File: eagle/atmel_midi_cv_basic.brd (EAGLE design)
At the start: 101 x 82 mm, 46 parts, among them IC1 TL074P, Q2 2N3904, U1 ATMEGA328P_PDIP

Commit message: led fixed
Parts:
- R11: value 1k -> 1k5
- R4: value 1k8 -> 3k3
- moved VEL_LED 1.80 mm to (28.4, 24.1)
- moved Q2 1.27 mm to (30.5, 17.8)
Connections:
- removed net N$47: R25.2, VEL_LED.K
- new net N$24: Q2.3, R25.2
- net N$20: now also Q2.1, VEL_LED.K; no longer Q2.3, VEL_LED.A
- net N$21: now also VEL_LED.A; no longer Q2.1
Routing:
- net N$47: track 6.83 -> 0.00 mm
- net N$24: track 0.00 -> 3.81 mm
- net N$21: track 43.2 -> 39.4 mm
- net N$20: track 5.47 -> 6.56 mm
- net N$23: track 6.83 -> 5.74 mm
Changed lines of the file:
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@@
 <?xml version="1.0" encoding="utf-8"?>
 <!DOCTYPE eagle SYSTEM "eagle.dtd">
-<eagle version="7.1.0">
+<eagle version="7.2.0">
 <drawing>
 <settings>
@@
 <attribute name="OC_FARNELL" value="1667008" x="55.88" y="69.85" size="1.778" layer="27" display="off"/>
 </element>
-<element name="Q2" library="transistor-npn" package="TO92" value="2N3904" x="29.21" y="17.78" rot="R180"/>
+<element name="Q2" library="transistor-npn" package="TO92" value="2N3904" x="30.48" y="17.78" rot="R180"/>
 <element name="R1" library="rcl" package="0207/10" value="10k" x="19.05" y="67.31"/>
 <element name="R10" library="rcl" package="0207/10" value="1k" x="72.39" y="20.32"/>
-<element name="R11" library="rcl" package="0207/10" value="1k" x="46.355" y="45.466" rot="R180"/>
+<element name="R11" library="rcl" package="0207/10" value="1k5" x="46.355" y="45.466" rot="R180"/>
 <element name="R17" library="rcl" package="0207/10" value="10k" x="40.64" y="21.59" rot="R180"/>
 <element name="R18" library="rcl" package="0207/10" value="47k" x="37.338" y="27.686"/>
@@
 <element name="R26" library="rcl" package="0207/10" value="1k" x="19.05" y="37.084"/>
 <element name="R3" library="rcl" package="0207/10" value="270" x="74.93" y="46.99" rot="R180"/>
-<element name="R4" library="rcl" package="0207/10" value="1k8" x="40.64" y="13.716"/>
+<element name="R4" library="rcl" package="0207/10" value="3k3" x="40.64" y="13.716"/>
 <element name="R5" library="rcl" package="0207/10" value="3.3k" x="32.258" y="42.672" rot="R270"/>
 <element name="R6" library="pot" package="B64W" value="10k" x="53.34" y="25.4" rot="R90"/>
@@
 <element name="U1" library="SparkFun-DigitalIC" package="DIL28-3" value="ATMEGA328P_PDIP" x="60.96" y="60.96" rot="R180"/>
 <element name="VEL" library="erthenvar" package="ERTHENVAR-JACK-90DEG" value="AUDIO-JACK" x="66.04" y="0" rot="R180"/>
-<element name="VEL_LED" library="SparkFun-LED" package="LED5MM" value="" x="29.718" y="22.86"/>
+<element name="VEL_LED" library="SparkFun-LED" package="LED5MM" value="" x="28.448" y="24.13"/>
 </elements>
 <signals>
@@
 <wire x1="35.052" y1="55.118" x2="41.402" y2="60.198" width="0.8128" layer="16"/>
 </signal>
-<signal name="N$47">
-<contactref element="R25" pad="2"/>
-<contactref element="VEL_LED" pad="K"/>
-<wire x1="30.988" y1="22.86" x2="35.56" y2="17.78" width="0.8128" layer="16"/>
-</signal>
 <signal name="N$14">
 <contactref element="U$4" pad="6"/>
@@
 <wire x1="64.77" y1="57.15" x2="66.04" y2="53.34" width="0.8128" layer="16"/>
 </signal>
-<signal name="N$20">
-<contactref element="VEL_LED" pad="A"/>
-<contactref element="Q2" pad="3"/>
-<wire x1="28.448" y1="22.86" x2="30.48" y2="17.78" width="0.8128" layer="16"/>
-</signal>
 <signal name="N$21">
 <contactref element="IC1" pad="14"/>
-<contactref element="Q2" pad="1"/>
 <contactref element="IC1" pad="13"/>
-<wire x1="21.59" y1="25.4" x2="27.94" y2="17.78" width="0.8128" layer="16"/>
 <wire x1="21.209" y1="26.035" x2="21.59" y2="25.4" width="0.8128" layer="16"/>
 <wire x1="21.209" y1="40.005" x2="21.209" y2="26.035" width="0.8128" layer="16"/>
@@
 <wire x1="36.576" y1="41.91" x2="35.179" y2="41.148" width="0.8128" layer="16"/>
 <wire x1="36.576" y1="41.91" x2="39.116" y2="41.91" width="0.8128" layer="16"/>
+<contactref element="VEL_LED" pad="A"/>
+<wire x1="27.178" y1="24.13" x2="22.86" y2="24.13" width="0.8128" layer="16"/>
+<wire x1="22.86" y1="24.13" x2="21.59" y2="25.4" width="0.8128" layer="16"/>
 </signal>
 <signal name="N$22">
@@
 <contactref element="Q2" pad="2"/>
 <contactref element="R4" pad="1"/>
-<wire x1="33.274" y1="13.843" x2="29.21" y2="15.875" width="0.8128" layer="16"/>
+<wire x1="33.274" y1="13.843" x2="30.48" y2="15.875" width="0.8128" layer="16"/>
 <wire x1="35.56" y1="13.716" x2="33.274" y2="13.843" width="0.8128" layer="16"/>
 </signal>
@@
 <wire x1="65.024" y1="20.574" x2="67.31" y2="20.32" width="0.8128" layer="16"/>
 </signal>
+<signal name="N$20">
+<contactref element="Q2" pad="1"/>
+<contactref element="VEL_LED" pad="K"/>
+<wire x1="29.21" y1="17.78" x2="29.21" y2="23.622" width="0.8128" layer="16"/>
+<wire x1="29.21" y1="23.622" x2="29.718" y2="24.13" width="0.8128" layer="16"/>
+</signal>
+<signal name="N$24">
+<contactref element="Q2" pad="3"/>
+<contactref element="R25" pad="2"/>
+<wire x1="35.56" y1="17.78" x2="31.75" y2="17.78" width="0.8128" layer="16"/>
+</signal>
 </signals>

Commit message: playing scale to indicate midi channel by number of notes
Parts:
- R5: value 3.3k -> 3k3
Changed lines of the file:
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@@
 <?xml version="1.0" encoding="utf-8"?>
 <!DOCTYPE eagle SYSTEM "eagle.dtd">
-<eagle version="7.2.0">
+<eagle version="7.1.0">
 <drawing>
 <settings>
@@
 <element name="R3" library="rcl" package="0207/10" value="270" x="74.93" y="46.99" rot="R180"/>
 <element name="R4" library="rcl" package="0207/10" value="3k3" x="40.64" y="13.716"/>
-<element name="R5" library="rcl" package="0207/10" value="3.3k" x="32.258" y="42.672" rot="R270"/>
+<element name="R5" library="rcl" package="0207/10" value="3k3" x="32.258" y="42.672" rot="R270"/>
 <element name="R6" library="pot" package="B64W" value="10k" x="53.34" y="25.4" rot="R90"/>
 <element name="R7" library="rcl" package="0207/10" value="5k" x="59.69" y="33.02" rot="R90"/>

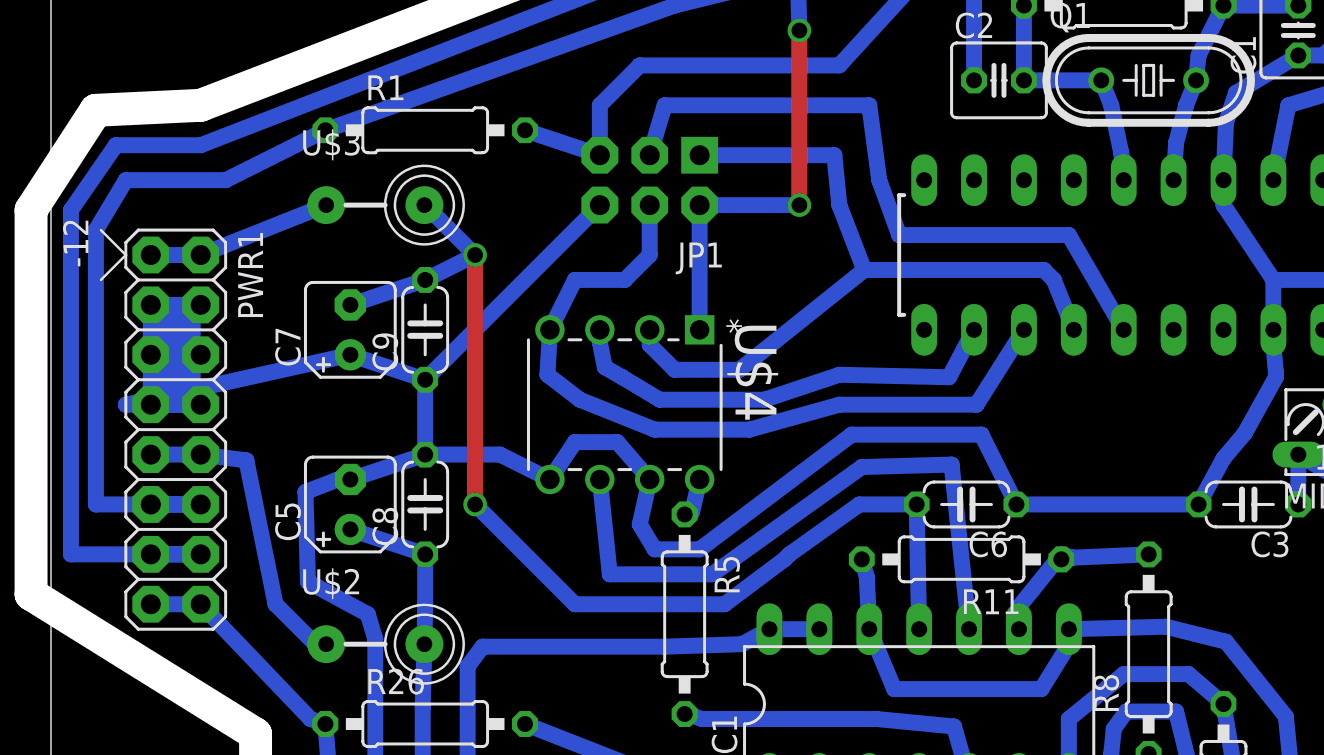
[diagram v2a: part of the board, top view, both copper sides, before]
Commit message: no neg supply
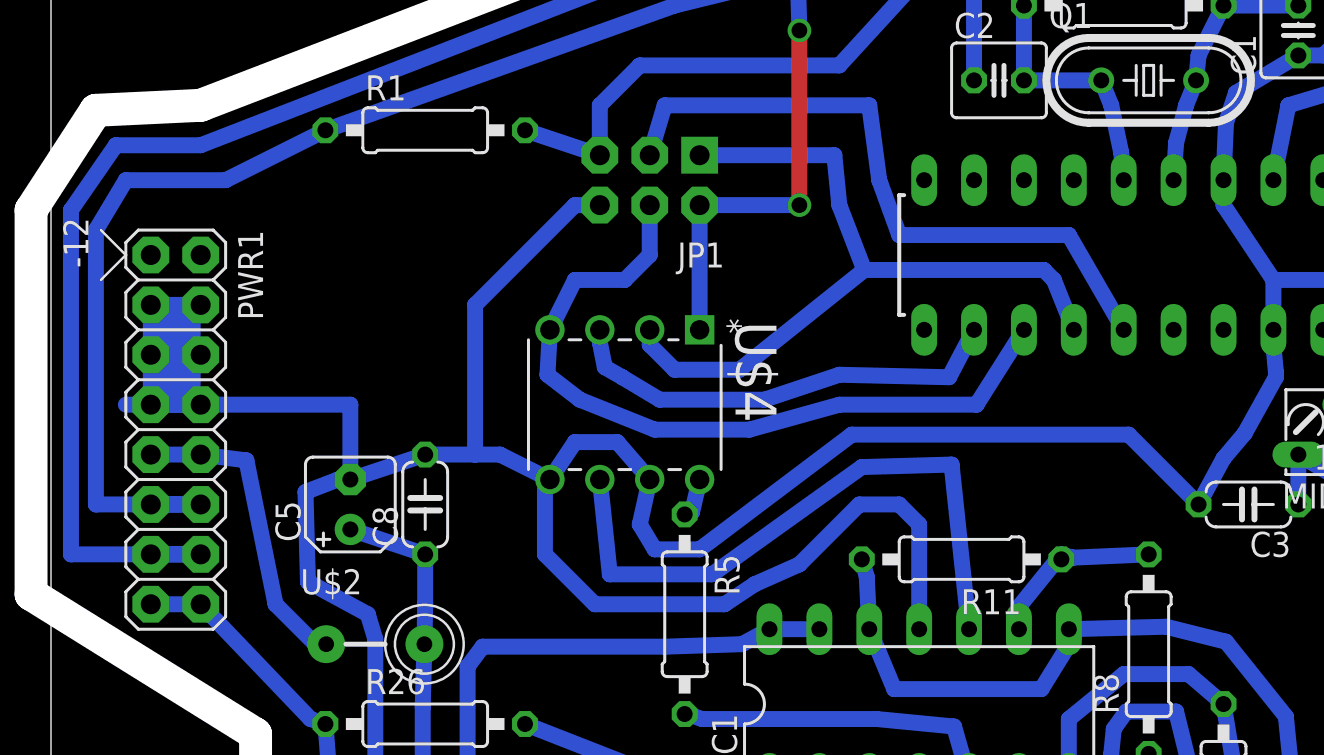
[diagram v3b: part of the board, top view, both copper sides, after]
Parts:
- removed C6, C9: 100n, rcl:C050-024X044
- removed C7: 10u, rcl:B45181A
- removed U$3: FB, adafruit:FB
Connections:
- removed net -12V: C6.2, C7.-, C9.2, IC1.11, U$3.P$2
- removed net N$18: PWR1.1, PWR1.2, U$3.P$1
- net GND: now also IC1.11; no longer C6.1, C7.+, C9.1
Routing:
- net -12V: track 55.8 -> 0.00 mm, vias 2 -> 0
- net GND: track 379.8 -> 406.0 mm
- net N$18: track 9.42 -> 0.00 mm
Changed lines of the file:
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@@
 <element name="C4" library="rcl" package="C050-024X044" value="100n" x="45.72" y="30.226"/>
 <element name="C5" library="rcl" package="B45181A" value="10u" x="15.24" y="48.26" rot="R90"/>
-<element name="C6" library="rcl" package="C050-024X044" value="100n" x="46.609" y="48.26" rot="R180"/>
-<element name="C7" library="rcl" package="B45181A" value="10u" x="15.24" y="57.15" rot="R90"/>
 <element name="C8" library="rcl" package="C050-024X044" value="100n" x="19.05" y="48.26" rot="R90"/>
-<element name="C9" library="rcl" package="C050-024X044" value="100n" x="19.05" y="57.15" rot="R90"/>
 <element name="D1" library="diode" package="DO35-10" value="1N4148DO35-10" x="72.39" y="29.21"/>
 <element name="GATE" library="erthenvar" package="ERTHENVAR-JACK-90DEG" value="AUDIO-JACK" x="20.828" y="0" rot="R180"/>
@@
 <element name="RST2" library="wirepad" package="2,54/0,9" value="reset " x="78.74" y="53.34"/>
 <element name="U$2" library="adafruit" package="FB" value="FB" x="16.51" y="41.148"/>
-<element name="U$3" library="adafruit" package="FB" value="FB" x="16.51" y="63.5"/>
 <element name="U$4" library="MCP4822" package="DIP254P762X432-8" value="MCP4822-E/P" x="25.4" y="49.53" rot="R270">
 <attribute name="PACKAGE" value="DIP-8" x="25.4" y="49.53" size="1.778" layer="27" rot="R270" display="off"/>
@@
 <contactref element="PWR1" pad="8"/>
 <contactref element="C5" pad="-"/>
-<contactref element="C7" pad="+"/>
 <contactref element="C8" pad="2"/>
-<contactref element="C9" pad="1"/>
 <contactref element="GATE" pad="P$1"/>
 <contactref element="MIDI_CH" pad="E"/>
-<contactref element="C6" pad="1"/>
 <contactref element="C4" pad="2"/>
 <contactref element="VEL" pad="P$1"/>
 <contactref element="PITCH" pad="P$1"/>
-<wire x1="19.05" y1="54.61" x2="19.05" y2="50.8" width="0.8128" layer="16"/>
-<wire x1="19.05" y1="50.8" x2="22.86" y2="50.8" width="0.8128" layer="16"/>
+<wire x1="19.05" y1="50.8" x2="21.59" y2="50.8" width="0.8128" layer="16"/>
+<wire x1="21.59" y1="50.8" x2="22.86" y2="50.8" width="0.8128" layer="16"/>
 <wire x1="22.86" y1="50.8" x2="25.4" y2="49.53" width="0.8128" layer="16"/>
 <wire x1="28.829" y1="51.435" x2="30.48" y2="49.53" width="0.8128" layer="16"/>
@@
 <wire x1="25.4" y1="49.53" x2="26.67" y2="51.435" width="0.8128" layer="16"/>
 <wire x1="19.05" y1="50.8" x2="15.24" y2="49.53" width="0.8128" layer="16"/>
-<wire x1="19.05" y1="54.61" x2="15.24" y2="55.88" width="0.8128" layer="16"/>
-<wire x1="19.05" y1="54.61" x2="27.94" y2="63.5" width="0.8128" layer="16"/>
 <wire x1="59.817" y1="67.691" x2="59.69" y2="64.77" width="0.8128" layer="16"/>
 <wire x1="60.325" y1="69.215" x2="59.817" y2="67.691" width="0.8128" layer="16"/>
@@
 <wire x1="62.23" y1="57.15" x2="62.23" y2="59.69" width="0.8128" layer="16"/>
 <wire x1="62.23" y1="59.69" x2="59.69" y2="63.5" width="0.8128" layer="16"/>
-<wire x1="47.371" y1="51.816" x2="40.767" y2="51.816" width="0.8128" layer="16"/>
 <wire x1="7.62" y1="58.42" x2="5.08" y2="58.42" width="0.8128" layer="16"/>
 <wire x1="5.08" y1="55.88" x2="5.08" y2="53.34" width="0.8128" layer="16"/>
@@
 <wire x1="16.59" y1="2.905375" x2="19.057509375" y2="2.832884375" width="0.8128" layer="16"/>
 <wire x1="7.62" y1="53.34" x2="3.81" y2="53.34" width="0.8128" layer="16"/>
-<wire x1="3.81" y1="53.34" x2="15.24" y2="55.88" width="0.8128" layer="16"/>
 <wire x1="46.99" y1="69.85" x2="46.99" y2="74.93" width="0.8128" layer="16"/>
 <wire x1="46.99" y1="74.93" x2="48.006" y2="75.438" width="0.8128" layer="16"/>
@@
 <wire x1="30.734" y1="45.974" x2="33.02" y2="45.974" width="0.8128" layer="16"/>
 <wire x1="33.02" y1="45.974" x2="40.767" y2="51.816" width="0.8128" layer="16"/>
-<wire x1="47.371" y1="51.816" x2="49.149" y2="48.26" width="0.8128" layer="16"/>
 <contactref element="R6" pad="E"/>
 <wire x1="48.26" y1="30.226" x2="55.118" y2="30.226" width="0.8128" layer="16"/>
@@
 <wire x1="19.057509375" y1="2.832884375" x2="34.662884375" y2="2.832884375" width="0.8128" layer="16"/>
 <wire x1="34.662884375" y1="2.832884375" x2="38.18" y2="3.81" width="0.8128" layer="16"/>
-<wire x1="49.149" y1="48.26" x2="58.42" y2="48.26" width="0.8128" layer="16"/>
 <wire x1="79.375" y1="55.245" x2="78.74" y2="53.34" width="0.8128" layer="16"/>
 <wire x1="78.74" y1="53.34" x2="76.327" y2="48.26" width="0.8128" layer="16"/>
+<contactref element="IC1" pad="11"/>
+<wire x1="7.62" y1="53.34" x2="15.24" y2="53.34" width="0.8128" layer="16"/>
+<wire x1="15.24" y1="53.34" x2="15.24" y2="49.53" width="0.8128" layer="16"/>
+<wire x1="27.94" y1="63.5" x2="26.67" y2="63.5" width="0.8128" layer="16"/>
+<wire x1="26.67" y1="63.5" x2="21.59" y2="58.42" width="0.8128" layer="16"/>
+<wire x1="21.59" y1="58.42" x2="21.59" y2="50.8" width="0.8128" layer="16"/>
+<wire x1="40.767" y1="51.816" x2="54.864" y2="51.816" width="0.8128" layer="16"/>
+<wire x1="54.864" y1="51.816" x2="58.42" y2="48.26" width="0.8128" layer="16"/>
+<wire x1="44.196" y1="41.91" x2="44.196" y2="47.244" width="0.8128" layer="16"/>
+<wire x1="44.196" y1="47.244" x2="43.18" y2="48.26" width="0.8128" layer="16"/>
+<wire x1="43.18" y1="48.26" x2="41.148" y2="48.26" width="0.8128" layer="16"/>
+<wire x1="41.148" y1="48.26" x2="38.1" y2="45.212" width="0.8128" layer="16"/>
+<wire x1="38.1" y1="45.212" x2="35.814" y2="44.196" width="0.8128" layer="16"/>
+<wire x1="35.814" y1="44.196" x2="34.29" y2="43.18" width="0.8128" layer="16"/>
+<wire x1="34.29" y1="43.18" x2="27.686" y2="43.18" width="0.8128" layer="16"/>
+<wire x1="27.686" y1="43.18" x2="25.146" y2="45.72" width="0.8128" layer="16"/>
+<wire x1="25.146" y1="45.72" x2="25.146" y2="49.276" width="0.8128" layer="16"/>
+<wire x1="25.146" y1="49.276" x2="25.4" y2="49.53" width="0.8128" layer="16"/>
 </signal>
 <signal name="+12V">
@@
 <wire x1="19.05" y1="43.22" x2="19.01" y2="41.148" width="0.8128" layer="16"/>
 <wire x1="19.05" y1="45.72" x2="15.24" y2="46.99" width="0.8128" layer="16"/>
-</signal>
-<signal name="-12V">
-<contactref element="C7" pad="-"/>
-<contactref element="U$3" pad="P$2"/>
-<contactref element="C9" pad="2"/>
-<contactref element="C6" pad="2"/>
-<contactref element="IC1" pad="11"/>
-<wire x1="44.069" y1="48.26" x2="44.196" y2="41.91" width="0.8128" layer="16"/>
-<wire x1="44.069" y1="48.26" x2="41.148" y2="48.26" width="0.8128" layer="16"/>
-<wire x1="41.148" y1="48.26" x2="37.592" y2="45.72" width="0.8128" layer="16"/>
-<wire x1="37.592" y1="45.72" x2="37.338" y2="45.466" width="0.8128" layer="16"/>
-<wire x1="37.338" y1="45.466" x2="34.29" y2="43.18" width="0.8128" layer="16"/>
-<wire x1="34.29" y1="43.18" x2="26.67" y2="43.18" width="0.8128" layer="16"/>
-<wire x1="26.67" y1="43.18" x2="21.59" y2="48.26" width="0.8128" layer="16"/>
-<via x="21.59" y="48.26" extent="1-16" drill="0.8" shape="square"/>
-<wire x1="21.59" y1="48.26" x2="21.59" y2="60.96" width="0.8128" layer="1"/>
-<via x="21.59" y="60.96" extent="1-16" drill="0.8" shape="square"/>
-<wire x1="21.59" y1="60.96" x2="19.05" y2="59.69" width="0.8128" layer="16"/>
-<wire x1="15.24" y1="58.42" x2="19.05" y2="59.69" width="0.8128" layer="16"/>
-<wire x1="19.01" y1="63.5" x2="19.05" y2="63.5" width="0.8128" layer="16"/>
-<wire x1="19.05" y1="63.5" x2="21.59" y2="60.96" width="0.8128" layer="16"/>
 </signal>
 <signal name="N$2">
@@
 <wire x1="9.946" y1="50.506" x2="7.62" y2="50.8" width="0.8128" layer="16"/>
 </signal>
-<signal name="N$18">
-<contactref element="PWR1" pad="1"/>
-<contactref element="PWR1" pad="2"/>
-<contactref element="U$3" pad="P$1"/>
-<wire x1="7.62" y1="60.96" x2="5.08" y2="60.96" width="0.8128" layer="16"/>
-<wire x1="7.62" y1="60.96" x2="14.01" y2="63.5" width="0.8128" layer="16"/>
-</signal>
 <signal name="N$19">
